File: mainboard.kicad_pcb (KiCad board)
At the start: 2 copper layers, 81.3 x 72.5 mm, 57 parts, among them J1 Screw_Terminal_1x02, Q1 IRF9540N, U1 AT90CAN128-16MU, U2 MCP2551-I/SN, Y1 Crystal

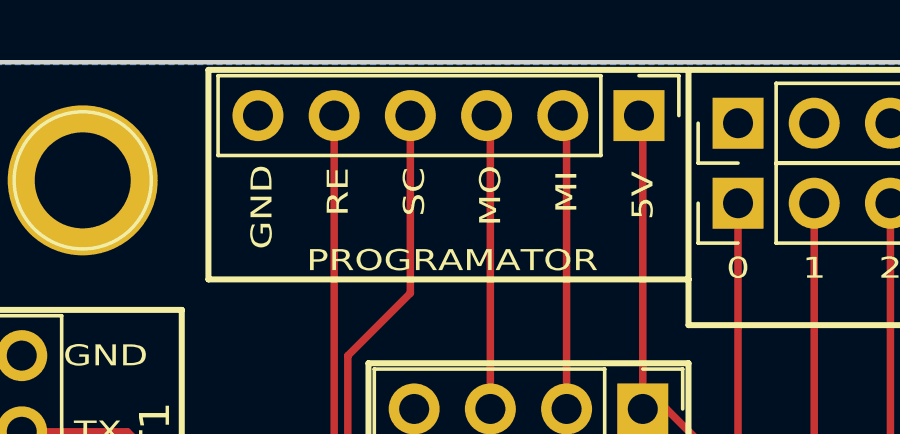
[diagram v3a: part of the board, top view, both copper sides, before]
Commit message: Removed some trases v3
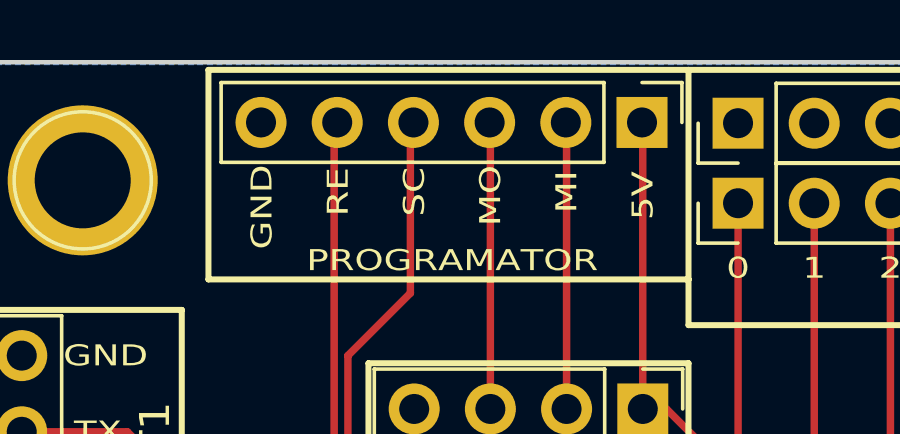
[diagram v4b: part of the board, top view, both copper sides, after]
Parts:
- moved PE_GND2 0.25 mm to (84.7, 39.0)
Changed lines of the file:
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@@
   )
   (module Pin_Headers:Pin_Header_Straight_1x06_Pitch2.54mm (layer F.Cu)
-    (at 84.582 38.735 270)
+    (at 84.6836 38.9636 270)
     (descr "Through hole straight pin header, 1x06, 2.54mm pitch, single row")
     (tags "Through hole pin header THT 1x06 2.54mm single row")
@@
     (effects (font (size 1 1) (thickness 0.1)))
   )
-  (segment (start 98.933 82.931) (end 98.933 86.717) (width 0.5) (layer F.Cu) (net 1) (status C00000))
-  (segment (start 98.933 86.717) (end 98.782 86.868) (width 0.5) (layer F.Cu) (net 1) (status C00000))
+  (segment (start 98.933 82.931) (end 98.933 86.717) (width 0.5) (layer F.Cu) (net 1))
+  (segment (start 98.933 86.717) (end 98.782 86.868) (width 0.5) (layer F.Cu) (net 1))
   (segment (start 98.782 86.868) (end 98.782 83.082) (width 0.25) (layer F.Cu) (net 1))
   (segment (start 98.782 83.082) (end 98.933 82.931) (width 0.25) (layer F.Cu) (net 1))
   (segment (start 101.162 78.82) (end 101.162 80.702) (width 0.25) (layer F.Cu) (net 1))
   (segment (start 101.162 80.702) (end 98.933 82.931) (width 0.25) (layer F.Cu) (net 1))
-  (segment (start 94.1366 99.8625) (end 99.1589 99.8625) (width 0.5) (layer F.Cu) (net 2) (status C00000))
-  (segment (start 99.1589 99.8625) (end 99.5553 100.2589) (width 0.5) (layer F.Cu) (net 2) (status C00000))
-  (segment (start 108.331 106.679) (end 112.683 106.679) (width 0.5) (layer F.Cu) (net 2) (status 400000))
-  (segment (start 112.683 106.679) (end 113.665 105.697) (width 0.5) (layer F.Cu) (net 2) (status 800000))
-  (segment (start 131.191 105.664) (end 131.191 105.407) (width 0.5) (layer F.Cu) (net 2) (status C00000))
-  (segment (start 131.191 105.407) (end 124.581 98.797) (width 0.5) (layer F.Cu) (net 2) (status C00000))
-  (segment (start 105.664 38.989) (end 109.7778 38.989) (width 0.5) (layer F.Cu) (net 2) (status C00000))
-  (segment (start 109.7778 38.989) (end 109.855 39.0662) (width 0.5) (layer F.Cu) (net 2) (status C00000))
-  (segment (start 115.443 39.0652) (end 117.426 39.0652) (width 0.5) (layer F.Cu) (net 2) (status C00000))
-  (segment (start 117.426 39.0652) (end 117.657 39.2962) (width 0.5) (layer F.Cu) (net 2) (status C00000))
-  (segment (start 66.675 101.6) (end 66.675 102.4382) (width 0.25) (layer F.Cu) (net 2) (status C00000))
-  (segment (start 66.675 102.4382) (end 68.4276 104.1908) (width 0.25) (layer F.Cu) (net 2) (status 400000))
+  (segment (start 94.1366 99.8625) (end 99.1589 99.8625) (width 0.5) (layer F.Cu) (net 2))
+  (segment (start 99.1589 99.8625) (end 99.5553 100.2589) (width 0.5) (layer F.Cu) (net 2))
+  (segment (start 108.331 106.679) (end 112.683 106.679) (width 0.5) (layer F.Cu) (net 2))
+  (segment (start 112.683 106.679) (end 113.665 105.697) (width 0.5) (layer F.Cu) (net 2))
+  (segment (start 131.191 105.664) (end 131.191 105.407) (width 0.5) (layer F.Cu) (net 2))
+  (segment (start 131.191 105.407) (end 124.581 98.797) (width 0.5) (layer F.Cu) (net 2))
+  (segment (start 105.664 38.989) (end 109.7778 38.989) (width 0.5) (layer F.Cu) (net 2))
+  (segment (start 109.7778 38.989) (end 109.855 39.0662) (width 0.5) (layer F.Cu) (net 2))
+  (segment (start 115.443 39.0652) (end 117.426 39.0652) (width 0.5) (layer F.Cu) (net 2))
+  (segment (start 117.426 39.0652) (end 117.657 39.2962) (width 0.5) (layer F.Cu) (net 2))
+  (segment (start 66.675 101.6) (end 66.675 102.4382) (width 0.25) (layer F.Cu) (net 2))
+  (segment (start 66.675 102.4382) (end 68.4276 104.1908) (width 0.25) (layer F.Cu) (net 2))
   (via (at 68.4276 104.1908) (size 0.6) (drill 0.4) (layers F.Cu B.Cu) (net 2))
-  (segment (start 99.1589 99.8625) (end 99.5553 100.2589) (width 0.25) (layer F.Cu) (net 2) (status C00000))
+  (segment (start 99.1589 99.8625) (end 99.5553 100.2589) (width 0.25) (layer F.Cu) (net 2))
   (segment (start 66.675 83.82) (end 66.675 83.312) (width 0.25) (layer F.Cu) (net 2))
   (segment (start 66.675 83.312) (end 64.008 80.645) (width 0.25) (layer F.Cu) (net 2))
@@
   (segment (start 117.657 39.2962) (end 115.674 39.2962) (width 0.25) (layer F.Cu) (net 2))
   (segment (start 115.674 39.2962) (end 115.443 39.0652) (width 0.25) (layer F.Cu) (net 2))
-  (segment (start 103.833 82.931) (end 103.833 86.818) (width 0.5) (layer F.Cu) (net 3) (status C00000))
-  (segment (start 103.833 86.818) (end 103.783 86.868) (width 0.5) (layer F.Cu) (net 3) (status C00000))
+  (segment (start 103.833 82.931) (end 103.833 86.818) (width 0.5) (layer F.Cu) (net 3))
+  (segment (start 103.833 86.818) (end 103.783 86.868) (width 0.5) (layer F.Cu) (net 3))
   (segment (start 103.783 86.868) (end 103.783 82.981) (width 0.25) (layer F.Cu) (net 3))
   (segment (start 103.783 82.981) (end 103.833 82.931) (width 0.25) (layer F.Cu) (net 3))
@@
   (segment (start 101.981 80.556) (end 101.981 81.079) (width 0.25) (layer F.Cu) (net 3))
   (segment (start 101.962 80.537) (end 101.981 80.556) (width 0.25) (layer F.Cu) (net 3))
-  (segment (start 108.331 98.626) (end 111.994 98.626) (width 0.5) (layer F.Cu) (net 4) (status 400000))
-  (segment (start 111.994 98.626) (end 113.665 100.297) (width 0.5) (layer F.Cu) (net 4) (status 800000))
-  (segment (start 113.665 100.297) (end 118.521 100.297) (width 0.5) (layer F.Cu) (net 4) (status 400000))
-  (segment (start 118.521 100.297) (end 120.021 98.797) (width 0.5) (layer F.Cu) (net 4) (status 800000))
-  (segment (start 121.666 42.164) (end 121.666 44.831) (width 0.5) (layer F.Cu) (net 4) (status C00000))
-  (segment (start 121.666 39.497) (end 121.666 42.164) (width 0.5) (layer F.Cu) (net 4) (status C00000))
+  (segment (start 108.331 98.626) (end 111.994 98.626) (width 0.5) (layer F.Cu) (net 4))
+  (segment (start 111.994 98.626) (end 113.665 100.297) (width 0.5) (layer F.Cu) (net 4))
+  (segment (start 113.665 100.297) (end 118.521 100.297) (width 0.5) (layer F.Cu) (net 4))
+  (segment (start 118.521 100.297) (end 120.021 98.797) (width 0.5) (layer F.Cu) (net 4))
+  (segment (start 121.666 42.164) (end 121.666 44.831) (width 0.5) (layer F.Cu) (net 4))
+  (segment (start 121.666 39.497) (end 121.666 42.164) (width 0.5) (layer F.Cu) (net 4))
   (segment (start 87.1601 101.6486) (end 87.1601 99.1235) (width 0.25) (layer F.Cu) (net 4))
   (segment (start 108.331 97.4598) (end 108.331 98.626) (width 0.25) (layer F.Cu) (net 4))
@@
   (segment (start 90.0176 106.7435) (end 89.6366 106.3625) (width 0.25) (layer F.Cu) (net 5))
   (segment (start 89.6366 106.3625) (end 89.6366 99.8625) (width 0.25) (layer F.Cu) (net 5))
-  (segment (start 124.206 42.164) (end 124.206 39.497) (width 0.5) (layer F.Cu) (net 6) (status C00000))
-  (segment (start 124.206 44.831) (end 124.206 42.164) (width 0.5) (layer F.Cu) (net 6) (status C00000))
+  (segment (start 124.206 42.164) (end 124.206 39.497) (width 0.5) (layer F.Cu) (net 6))
+  (segment (start 124.206 44.831) (end 124.206 42.164) (width 0.5) (layer F.Cu) (net 6))
   (segment (start 124.714 49.878) (end 124.714 48.186) (width 0.25) (layer F.Cu) (net 6))
   (segment (start 124.714 48.186) (end 124.026 47.498) (width 0.25) (layer F.Cu) (net 6))
   (segment (start 124.026 47.498) (end 124.026 45.011) (width 0.25) (layer F.Cu) (net 6))
   (segment (start 124.026 45.011) (end 124.206 44.831) (width 0.25) (layer F.Cu) (net 6))
-  (segment (start 126.746 39.497) (end 126.746 42.164) (width 0.5) (layer F.Cu) (net 7) (status C00000))
-  (segment (start 126.746 42.164) (end 126.746 44.831) (width 0.5) (layer F.Cu) (net 7) (status C00000))
+  (segment (start 126.746 39.497) (end 126.746 42.164) (width 0.5) (layer F.Cu) (net 7))
+  (segment (start 126.746 42.164) (end 126.746 44.831) (width 0.5) (layer F.Cu) (net 7))
   (segment (start 125.984 49.878) (end 125.984 48.44) (width 0.25) (layer F.Cu) (net 7))
   (segment (start 125.984 48.44) (end 126.926 47.498) (width 0.25) (layer F.Cu) (net 7))
@@
   (segment (start 121.539 49.964) (end 123.358 49.964) (width 0.25) (layer F.Cu) (net 62))
   (segment (start 123.358 49.964) (end 123.444 49.878) (width 0.25) (layer F.Cu) (net 62))
-  (segment (start 108.331 101.526) (end 108.331 103.379) (width 0.5) (layer F.Cu) (net 63) (status C00000))
-  (segment (start 122.301 105.097) (end 128.084 105.097) (width 0.5) (layer F.Cu) (net 64) (status C00000))
-  (segment (start 128.084 105.097) (end 128.651 105.664) (width 0.5) (layer F.Cu) (net 64) (status C00000))
+  (segment (start 108.331 101.526) (end 108.331 103.379) (width 0.5) (layer F.Cu) (net 63))
+  (segment (start 122.301 105.097) (end 128.084 105.097) (width 0.5) (layer F.Cu) (net 64))
+  (segment (start 128.084 105.097) (end 128.651 105.664) (width 0.5) (layer F.Cu) (net 64))
   (segment (start 128.084 105.097) (end 128.651 105.664) (width 0.25) (layer F.Cu) (net 64))
   (zone (net 2) (net_name GND) (layer B.Cu) (hatch edge 0.508)

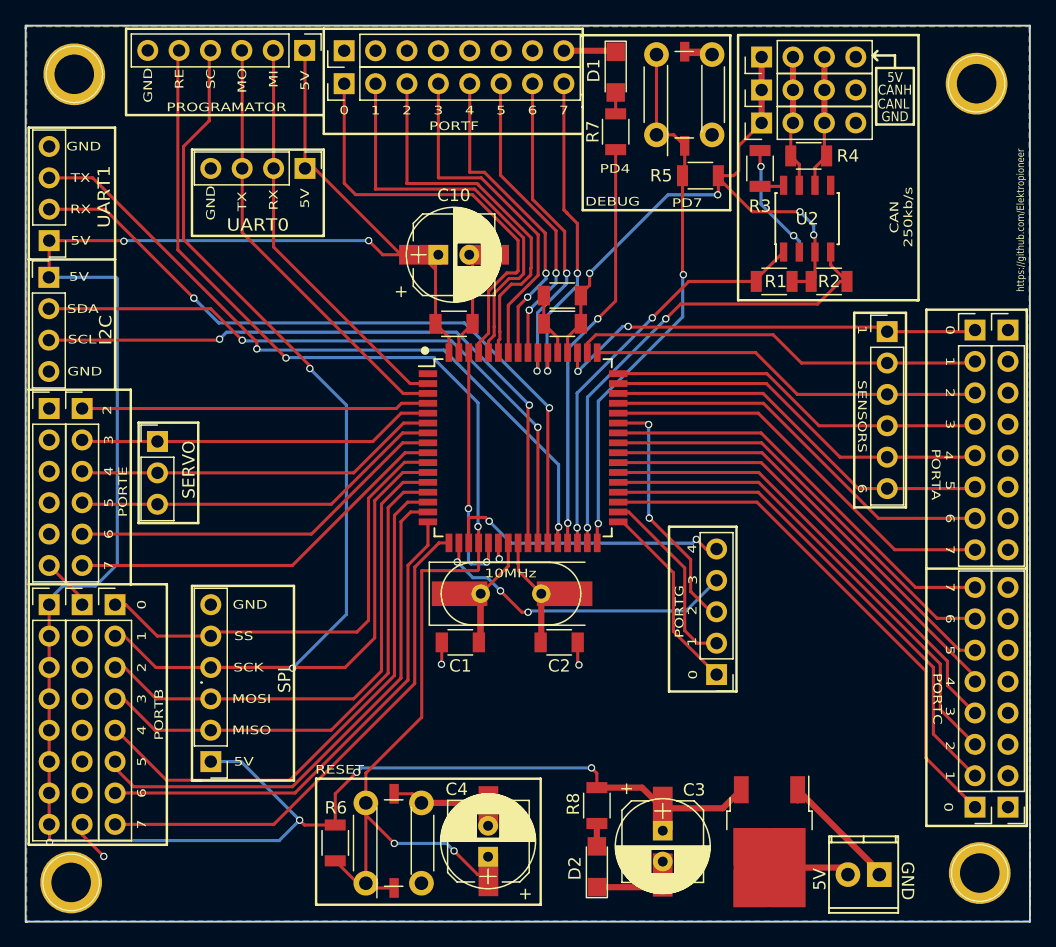
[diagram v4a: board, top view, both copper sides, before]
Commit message: Modified mosfet protection to smd
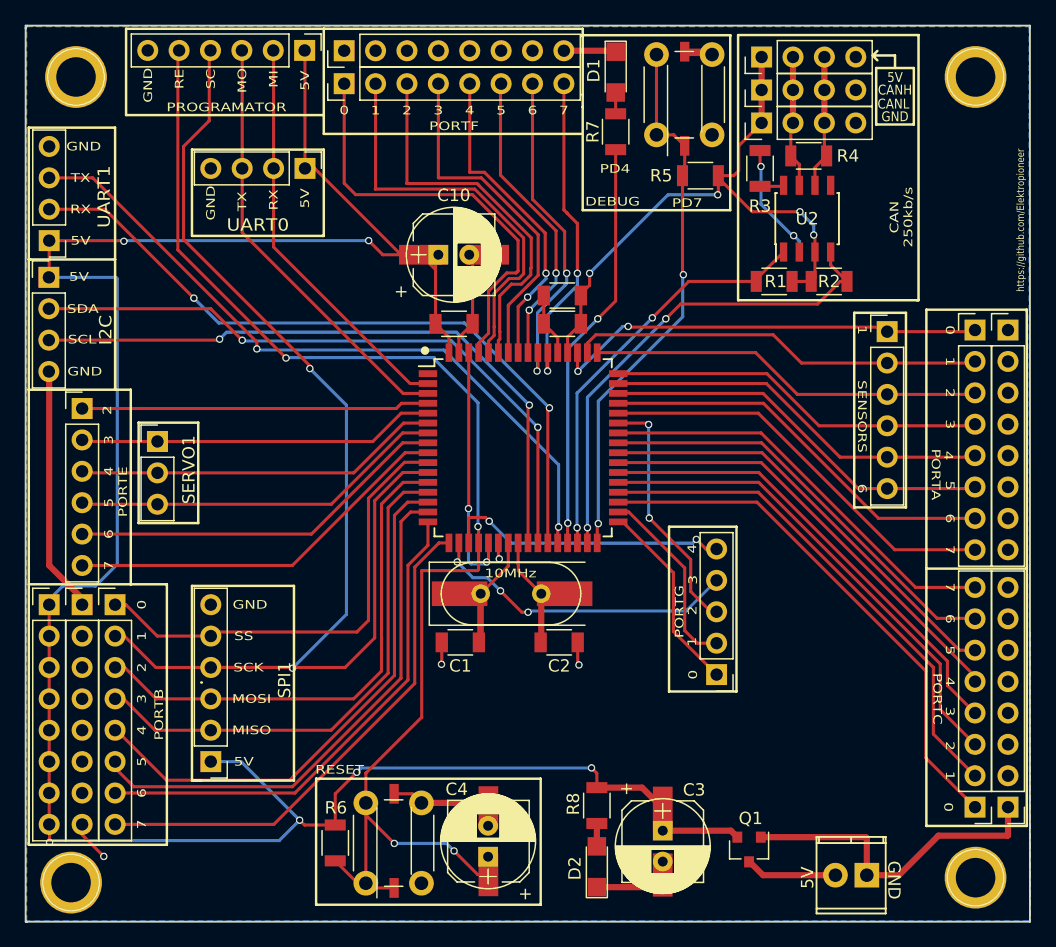
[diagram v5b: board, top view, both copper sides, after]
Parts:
- removed PE_GND1: CONN_01X06, Pin_Headers:Pin_Header_Straight_1x06_Pitch2.54mm
- removed the REF** at (66.0, 40.9)
- removed the REF** at (65.8, 106.3)
- removed the REF** at (139.1, 41.7)
- removed the REF** at (139.3, 105.5)
- added REF**: 1pin, Connectors:1pin, F.Cu at (139.0, 105.9)
- added REF**: 1pin, Connectors:1pin, F.Cu at (65.8, 106.3)
- added REF**: 1pin, Connectors:1pin, F.Cu at (66.2, 41.1)
- added REF**: 1pin, Connectors:1pin, F.Cu at (139.0, 41.1)
- Q1: value IRF9540N -> SQ2309ES; footprint TO_SOT_Packages_SMD:TO-252-2 -> TO_SOT_Packages_SMD:SOT-23
- moved Q1 1.77 mm to (120.7, 103.6)
- moved J1 1.01 mm to (130.2, 105.7)
- renumbered SERVO to SERVO1, SPI to SPI1
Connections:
- Q1 pad 2: Net-(J1-Pad2) -> +5V
- Q1 pad 3: +5V -> Net-(J1-Pad2)
- R8 pad 1: +5V -> (no net)
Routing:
- net GND: track 80.3 -> 106.5 mm
- net +5V: track 268.2 -> 265.4 mm
